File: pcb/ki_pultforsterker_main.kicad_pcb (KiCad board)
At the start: 2 copper layers, 180 x 100 mm, 264 parts, among them J1 24V IN, J10 LED-RINGER, J11 PC1, J12 PC2, J13 TFT, J15 USB1, J16 USB2, J17 USB3, J18 USB4, J19 USB PI, J2 SPK L, J20 AUX2, J21 PWR BAK, J22 EXP, J23 HODETLF, J24 NTC, J3 SPK R, J4 AUX1, J5 RPi 40-pin, J6 5V -> PI, J7 KNAPPER, J8 ENCODER, J9 OLED, K1 SRD-05VDC-SL-C, Q10 AO3401A, Q11 P-MOSFET 60V 20A (AOD409), Q2 AO3400A, Q3 AO3400A, Q4 AO3400A, Q5 AO3400A, Q6 AO3400A, Q7 AO3400A, Q8 AO3401A, Q9 AO3400A, U1 TPS54560DDAR, U10 PCM1808PWR, U11 PCM2900CDB, U12 MCP23017-E/SS, U13 TPA6132A2RTER, U14 74LVC1G14, U2 AMS1117-3.3, U3 LM2662MX, U4 PCM5102APWR, U5 PGA2311UA, U6 TPA3116D2DADR, U7 FE1.1s, U8 TS3USB221RSER, U9 AMS1117-3.3, X1 12.288MHz, Y1 12MHz, Y2 12MHz

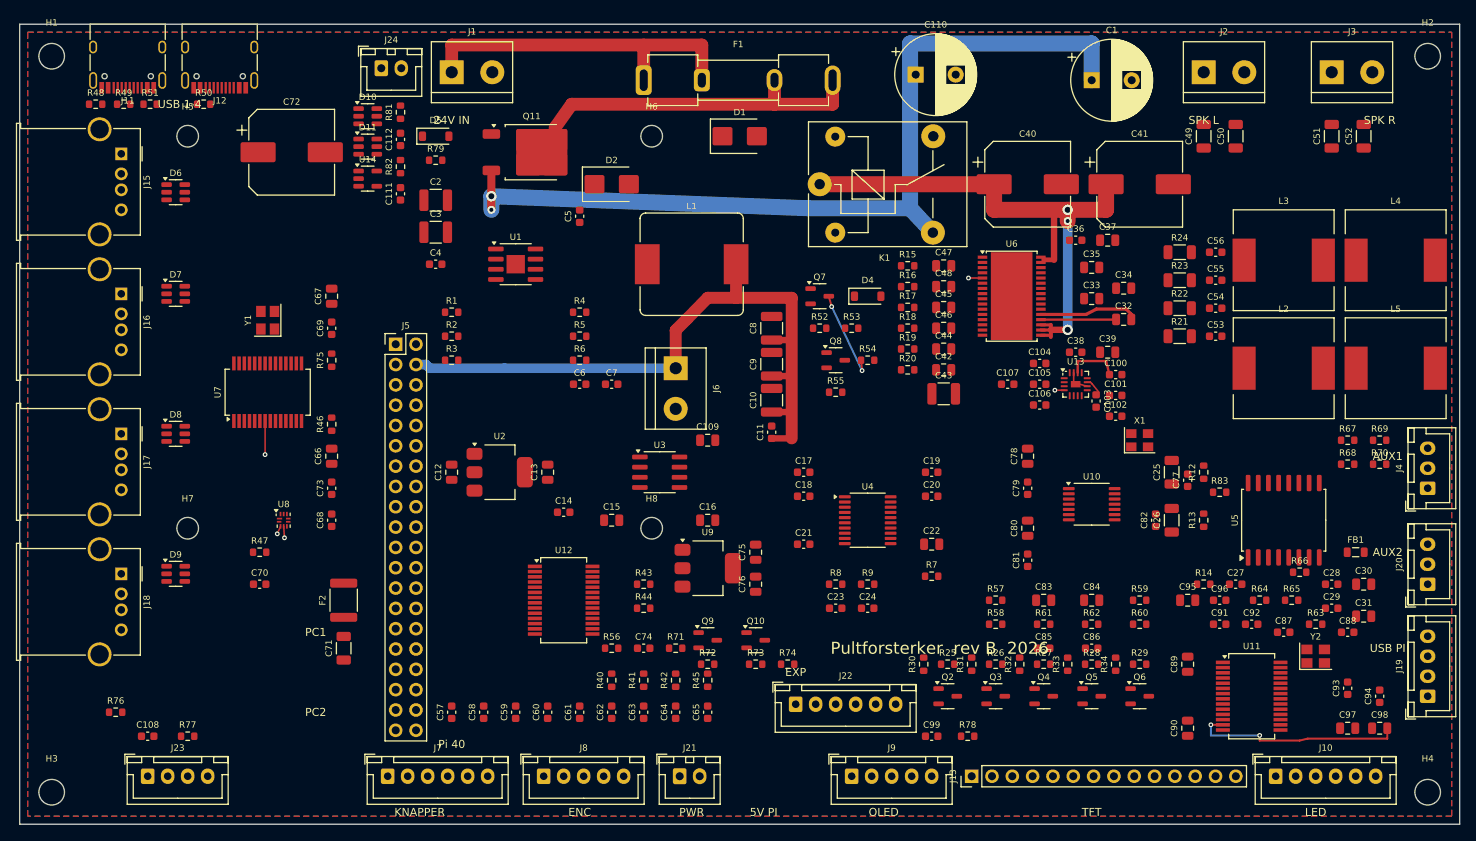
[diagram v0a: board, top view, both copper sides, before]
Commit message: PCB rev B: ny ruting etter sluttkontroll – DRC uten klarings-, hull-, kant- eller koblingsfeil; produksjonsfiler regenerert
Co-Authored-By: Claude Fable 5.1 <noreply@anthropic.com>
Claude-Session: https://claude.ai/code/session_01FaJKmYinw8SWRobKXBRYpt
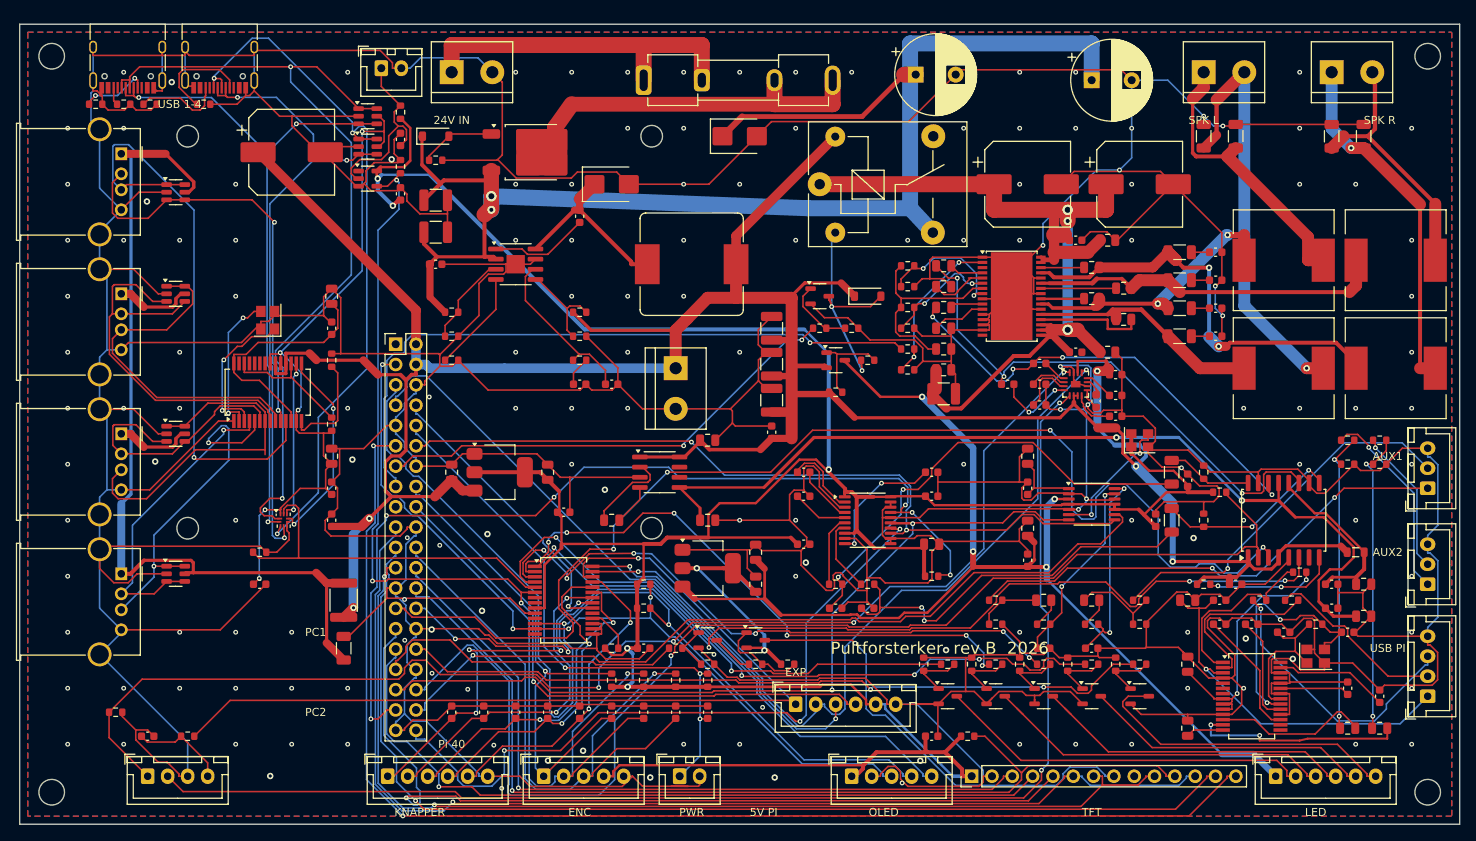
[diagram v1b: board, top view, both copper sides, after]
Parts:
- turned C32 to 180 degrees
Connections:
- J11 pad : GND -> (no net)
- J12 pad : GND -> (no net)
- U1 pad : GND -> (no net)
- U13 pad : GND -> (no net)
- U6 pad : GND -> (no net)
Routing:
- net GND: track 2.11 -> 1755.9 mm, vias 0 -> 156
- net 3V3: track 0.00 -> 394.9 mm, vias 0 -> 5
- net 5V: track 92.1 -> 387.2 mm, vias 0 -> 5
- net HP_OUTR: track 0.00 -> 161.8 mm, vias 0 -> 2
- net HP_OUTL: track 0.00 -> 159.6 mm, vias 0 -> 4
- net TOUCH_IRQ: track 0.00 -> 157.8 mm, vias 0 -> 2
- net PGA_CS: track 0.00 -> 151.9 mm, vias 0 -> 1
- net PGA_SDI: track 0.00 -> 151.5 mm, vias 0 -> 4
- net 5V_SW: track 0.00 -> 146.3 mm, vias 0 -> 4
- net SPI_MOSI: track 0.00 -> 140.4 mm, vias 0 -> 1
- net SPI_MISO: track 0.00 -> 136.8 mm, vias 0 -> 1
- net PGA_SCLK: track 0.00 -> 132.9 mm, vias 0 -> 5
- net SPI_SCLK: track 0.00 -> 130.9 mm, vias 0 -> 2
- net 5V_USB: track 0.00 -> 130.6 mm
- net EXP_B5: track 0.00 -> 130.2 mm, vias 0 -> 4
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
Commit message: PCB rev B: BOM/CPL regenerert med koder på lager hos JLCPCB, én linje per kode
Co-Authored-By: Claude Fable 5.1 <noreply@anthropic.com>
Claude-Session: https://claude.ai/code/session_01FaJKmYinw8SWRobKXBRYpt
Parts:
- C108, C11, C111, C112, C14, C20, C21, C27, C28, C29, C5, C57, C58, C59, C60, C61, C62, C63, C64, C65, C68, C69, C70, C73, C74, C77, C79, C81, C82, C96, C99: value 100n -> 100n/50V
- C44, C45, C46, C47, C48: value 1u -> 1u/50V
- D2: value SS56 (SMB) -> SS56
- D5: value BZT52C12 12V -> BZT52C12
- J11: value PC1 -> USB-C 16P
- J12: value PC2 -> USB-C 16P
- L2, L3, L4, L5: value 10uH 4A -> 10uH 5.5A
- Q11: value P-MOSFET 60V 20A (AOD409) -> AOD409
- R21, R22, R23, R24: value 18R 1206 -> 18R
- U14: value 74LVC1G14 -> SN74LVC1G14DBVR

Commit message: PCB rev B: produksjonsfiler med Littelfuse 111-sikringsklips (F1) – DRC ren; skjema regenerert
Co-Authored-By: Claude Fable 5.1 <noreply@anthropic.com>
Claude-Session: https://claude.ai/code/session_01FaJKmYinw8SWRobKXBRYpt
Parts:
- F1: value 5A 5x20 (Keystone 3512-klips) -> 5A 5x20 (Littelfuse 111-klips); footprint Fuseholder_Clip-5x20mm_Keystone_3512P_Inline_P23.62x7.27mm_D1.02x2.41x1.02x1.57mm_Horizontal -> Fuseholder_Clip-5x20mm_Littelfuse_111_Inline_P20.00x5.00mm_D1.05mm_Horizontal
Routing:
- net 24V_F: track 54.3 -> 50.7 mm
- net 24V_IN: track 43.5 -> 41.2 mm
- net GND: vias 156 -> 153

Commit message: PCB rev B: ny ruting etter rettelser av U4/U7/U8/U1 – DRC ren, gerber/BOM/CPL/skjema regenerert, CPL-rotasjon for TI-footprints, C1/C110 680–1000 µF
Co-Authored-By: Claude Opus 5.5 <noreply@anthropic.com>
Claude-Session: https://claude.ai/code/session_01FaJKmYinw8SWRobKXBRYpt
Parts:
- C1, C110: value 1000u/35V h<=16 -> 680-1000u/35V 10x16
- U1: footprint HSOP-8-1EP_3.9x4.9mm_P1.27mm_EP2.3x2.3mm -> Texas_HSOP-8-1EP_3.9x4.9mm_P1.27mm
- U7: footprint SSOP-28_5.3x10.2mm_P0.65mm -> SSOP-28_3.9x9.9mm_P0.635mm
- U8: footprint UQFN-10_1.4x1.8mm_P0.4mm -> Texas_UQFN-10_1.5x2mm_P0.5mm
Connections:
- U4 pad 10: DAC_LDOO -> GND
- U4 pad 18: GND -> DAC_LDOO
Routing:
- net 3V3: track 394.9 -> 341.2 mm, vias 5 -> 2
- net PGA_SDI: track 151.5 -> 177.9 mm
- net SPI_MOSI: track 140.4 -> 117.4 mm
- net USB1_DP: track 73.6 -> 50.6 mm, vias 1 -> 2
- net USB_XOUT: track 17.8 -> 40.7 mm, vias 2 -> 0
- net DAC_XSMT: track 116.0 -> 93.4 mm, vias 6 -> 3
- net SDA: track 103.7 -> 124.6 mm, vias 4 -> 2
- net USB2_DM: track 50.2 -> 30.6 mm, vias 0 -> 3
- net SPI_SCLK: track 130.9 -> 111.5 mm, vias 2 -> 1
- net GND: track 1755.9 -> 1774.1 mm, vias 153 -> 156
- net TOUCH_CS: track 124.5 -> 141.7 mm, vias 1 -> 2
- net USB3_DP: track 44.6 -> 27.9 mm, vias 0 -> 3
- net OLED_RES: track 91.4 -> 106.9 mm, vias 0 -> 2
- net HP_OUTL: track 159.6 -> 174.7 mm, vias 4 -> 2
- net ENC_SW: track 77.7 -> 63.2 mm, vias 1 -> 3
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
